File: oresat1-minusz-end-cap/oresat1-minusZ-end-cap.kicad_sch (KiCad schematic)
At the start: 36 parts, among them J1 M55-7011242R, J2 U.FL-R-SMA

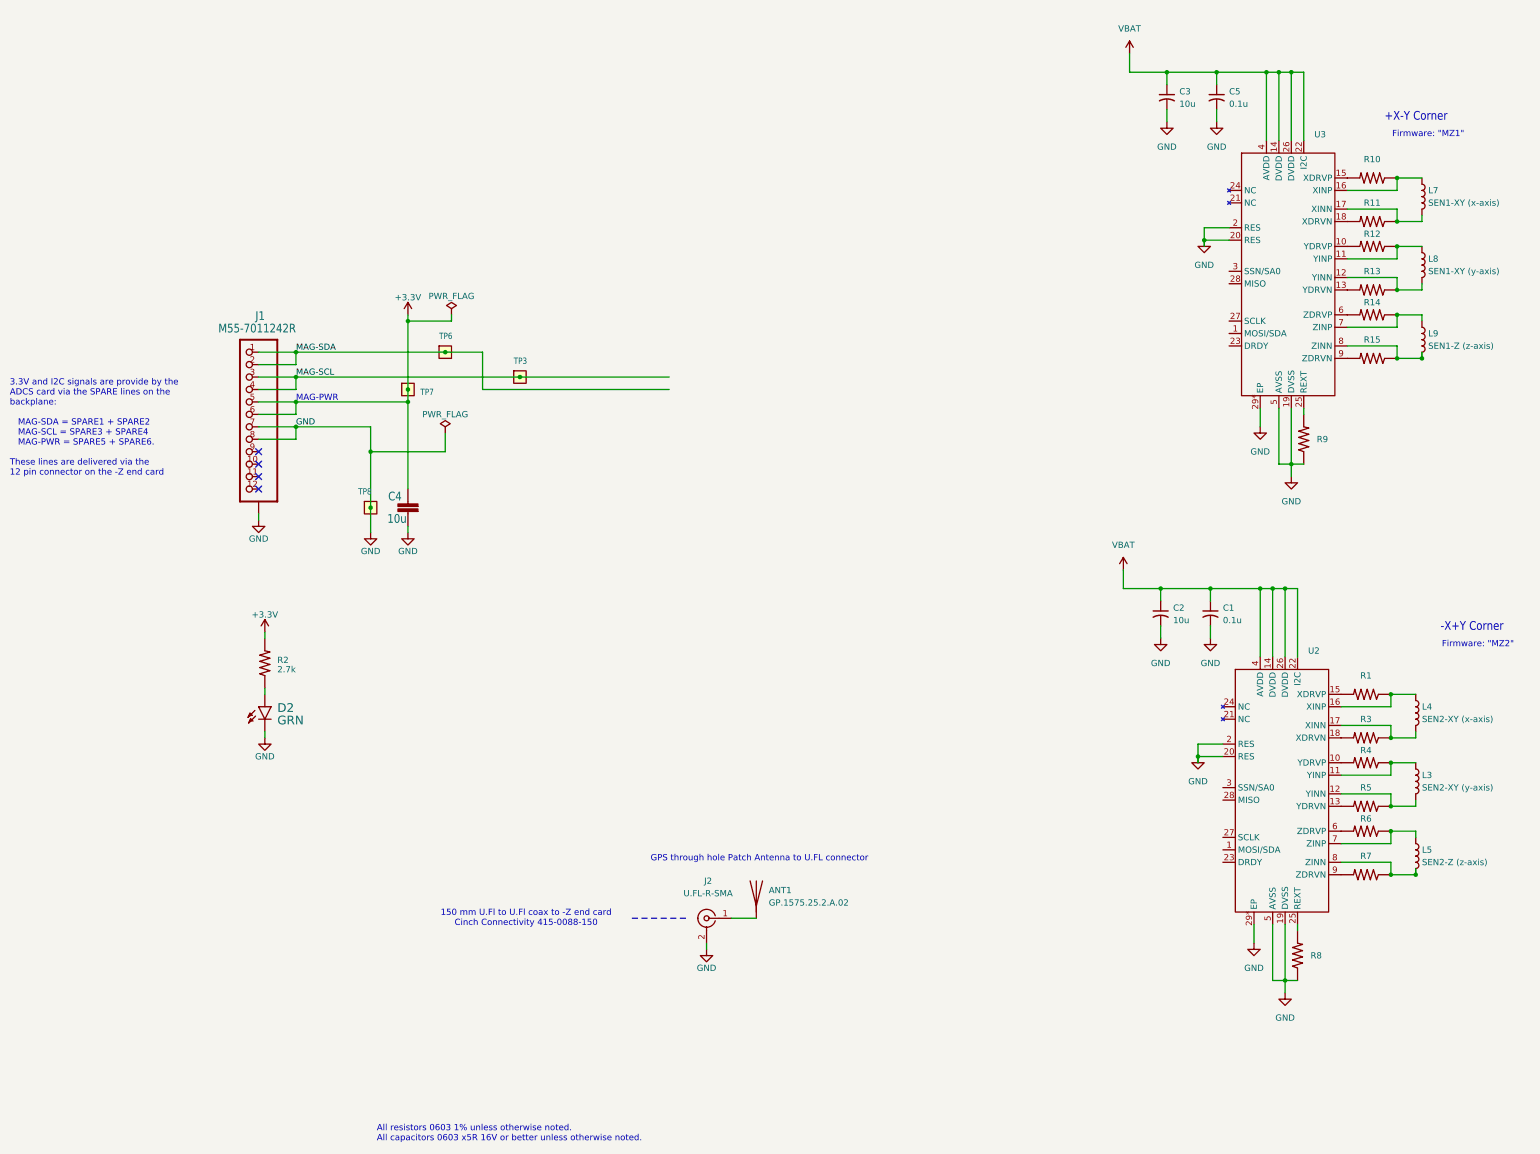
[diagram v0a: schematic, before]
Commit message: RM 3100 board layout
Round 1 - awaiting design review. Some issues with GND pads; DRC is clean, but looks weird. Debating if U1 needs to be further in the corner, therefore change its layout completely.
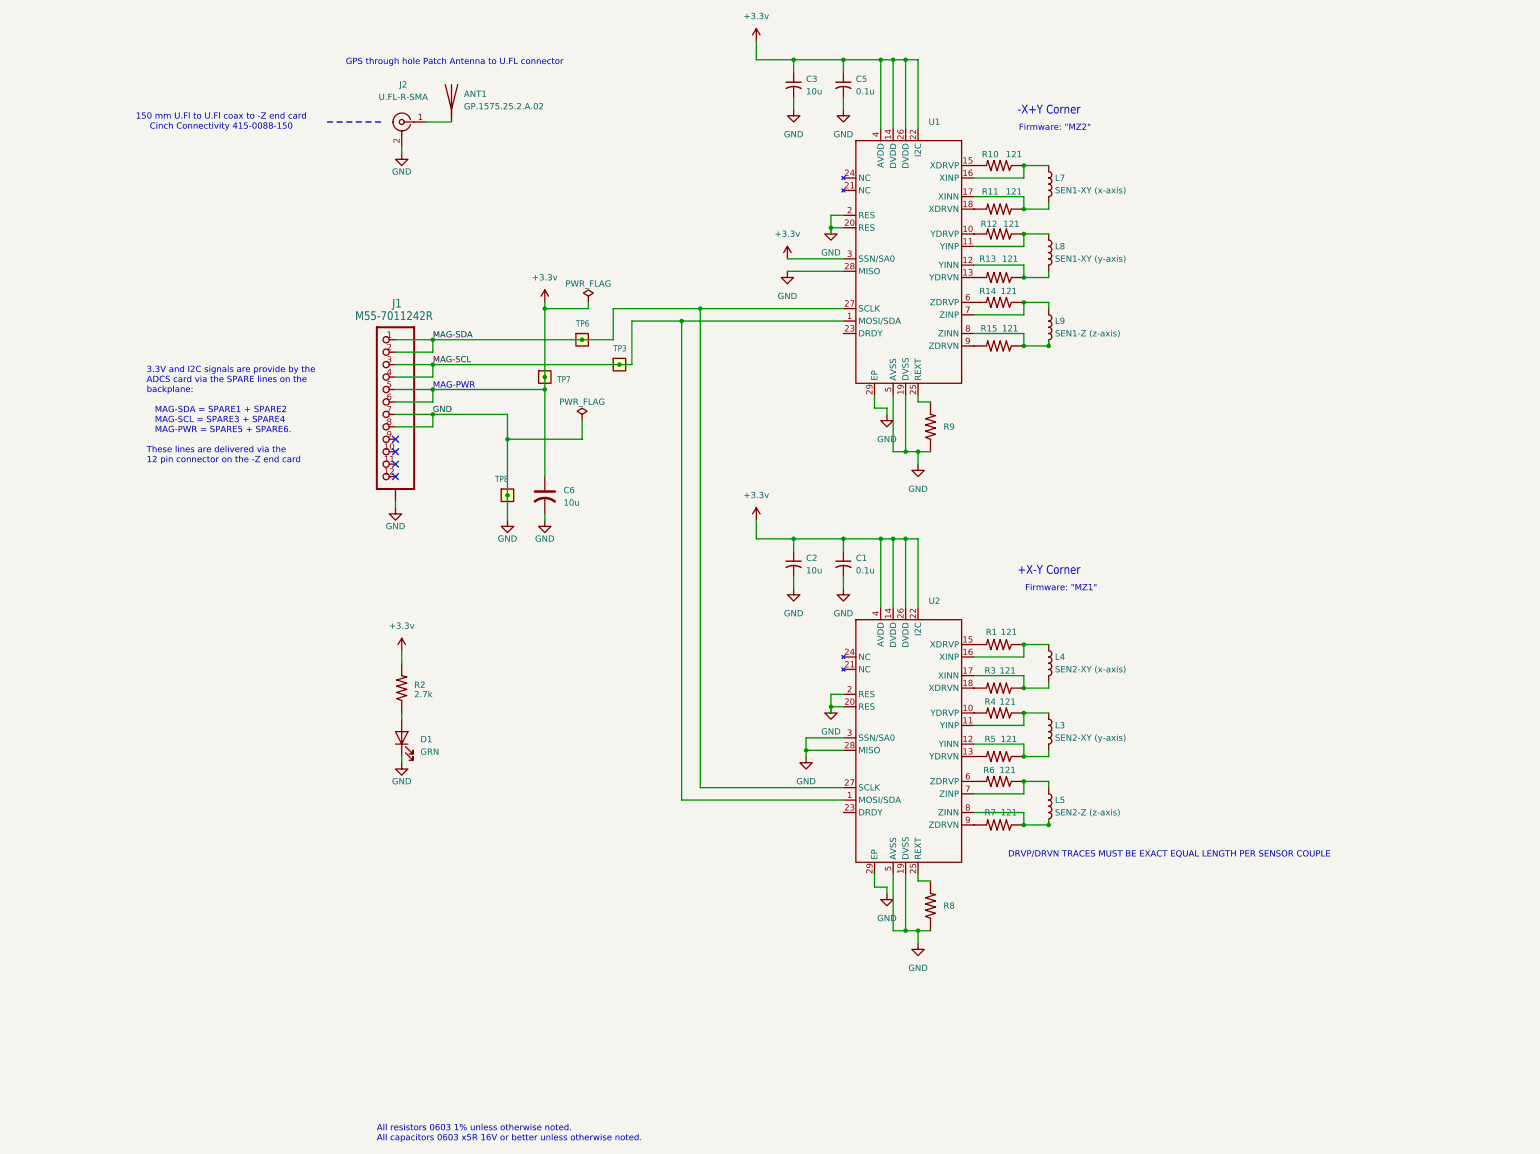
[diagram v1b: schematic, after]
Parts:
- removed C4: 10u, oresat-passives:0603-C-NOSILK, symbol oresat0.5-minusz-end-cap-eagle-import:C-EU0603-B-NOSILK
- removed D2: GRN, oresat-diodes:LED-0603, symbol oresat0.5-minusz-end-cap-eagle-import:LED-GREEN0603
- added C6: 10u, oresat-passives:0603-C-NOSILK, symbol Device:C_US
- added D1: GRN, oresat-passives:0603-C-NOSILK, symbol Device:LED
- C1, C2, C3, C5: footprint (none) -> oresat-passives:0603-C-NOSILK
- L3, L4, L7, L8: footprint (none) -> oresat-misc:RM3100 SEN-XY-f
- L5, L9: footprint (none) -> oresat-misc:RM3100 SEN-Z-f
- R1, R10, R11, R12, R13, R14, R15, R3, R4, R5, R6, R7: value ~ -> 121
- U1: renamed from U3; footprint (none) -> oresat-misc:RM3100-MagI2C
- U2: footprint (none) -> oresat-misc:RM3100-MagI2C
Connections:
- net +3.3V is gone; now on net +3.3v: J1.5, J1.6, R2.2, TP7.1
- net VBAT is gone; now on net +3.3v: C1.1, C2.1, C3.1, C5.1, U1.14 (DVDD), U1.22 (I2C), U1.26 (DVDD), U1.4 (AVDD), U2.14 (DVDD), U2.22 (I2C), U2.26 (DVDD), U2.4 (AVDD)
- net GND: now also U1.28 (MISO), U1.29 (EP), U2.28 (MISO), U2.29 (EP), U2.3 (SSN/SA0), C6.2, D1.1 (K); no longer U1.29* (EP), U2.29* (EP)
- net MAG-SCL: now also U1.1 (MOSI/SDA), U2.1 (MOSI/SDA)
- net MAG-SDA: now also U1.27 (SCLK), U2.27 (SCLK)
- net at R2.1: now also D1.2 (A)
- net +3.3v: now reaches U1.3 (SSN/SA0)
- net +3.3v: now also C6.1
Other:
- note added: "DRVP/DRVN TRACES MUST BE EXACT EQUAL LENGTH PER SENSOR COUPLE"
- moved on the sheet: ANT1, C1, C2, C3, C5, J1, J2, L3, L4, L5, L7, L8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

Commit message: Polishing the schematic and layout
Cleaned up ERCs, lots of OCD polishing for no reason, added 3.3V zone, cleaned up 3.3V routing.
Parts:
- added C4, C7: 100n, oresat-passives:0603-C-NOSILK, symbol Device:C_Small
- C1, C5: value 0.1u -> 100n; symbol Device:C_Small_US -> Device:C_Small
- C2: value 10u -> ~; footprint oresat-passives:0603-C-NOSILK -> oresat-passives:0805-C-NOSILK; symbol Device:C_Small_US -> Device:C_Small
- C3: footprint oresat-passives:0603-C-NOSILK -> oresat-passives:0805-C-NOSILK; symbol Device:C_Small_US -> Device:C_Small
- C6: footprint oresat-passives:0603-C-NOSILK -> oresat-passives:0805-C-NOSILK; symbol Device:C_US -> Device:C_Small
- J1: symbol oresat0.5-minusz-end-cap-eagle-import:J-HARWIN-M55-70X1242R -> oresat-connectors:J-HARWIN-M55-6001242R
- R8, R9: value ~ -> 33k
- U1, U2: value ~ -> RM3100
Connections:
- net +3.3v: now also U1.28 (MISO), C4.1, C7.1; no longer U1.3 (SSN/SA0)
- net GND: now also J1.SH (SHIELD), U1.3 (SSN/SA0), C4.2, C7.2; no longer J1.P$1 (SHIELDS), J1.P$2 (SHIELDS), J1.P$3 (SHIELDS), J1.P$4 (SHIELDS), U1.28 (MISO)
- no-connect marks 4 -> 6
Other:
- note added: "Address: 00"
- note added: "Address: 01"
- moved on the sheet: C1, C2, C3, J1

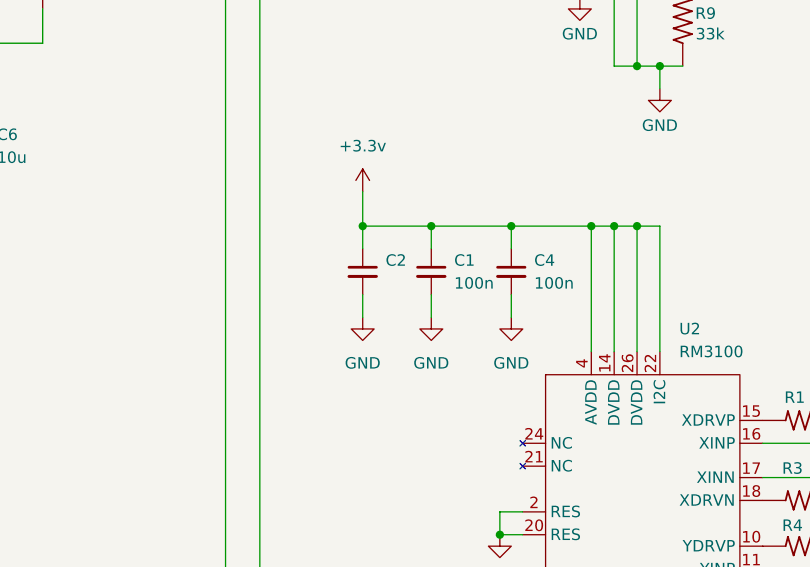
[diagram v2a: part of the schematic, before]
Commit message: Fix BOM and add 3D of antenna.
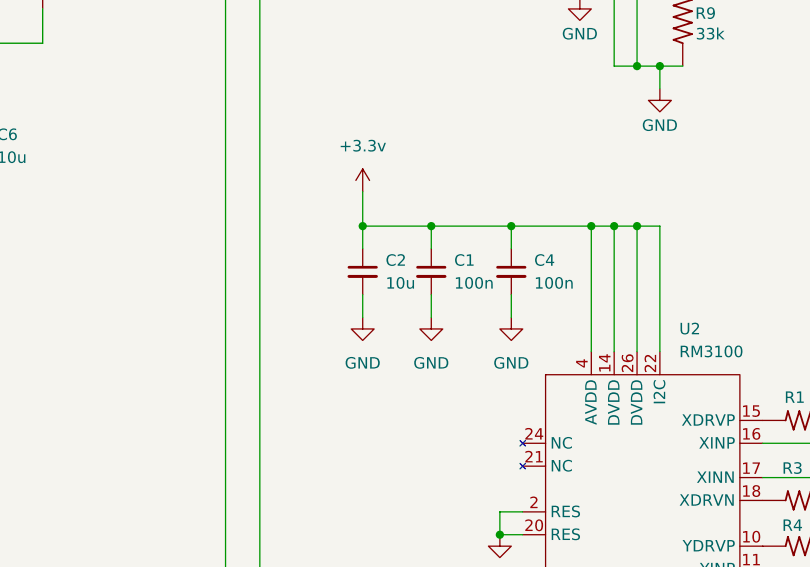
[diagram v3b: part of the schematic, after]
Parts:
- ANT1, J1, J2: DIS (none) -> DigiKey; DST Digi-Key -> (none)
- C1, C4, C5, C7: DIS (none) -> DigiKey; DPN (none) -> 399-6856-1-ND; MFR (none) -> KEMET; MPN (none) -> C0603C104K5RACAUTO
- C2: value ~ -> 10u; DIS (none) -> DigiKey; DPN (none) -> 490-GRT21BC71E106KE13KCT-ND; MFR (none) -> Murata Electronics; MPN (none) -> GRT21BC71E106KE13K
- C3, C6: DIS (none) -> DigiKey; DPN (none) -> 490-GRT21BC71E106KE13KCT-ND; MFR (none) -> Murata Electronics; MPN (none) -> GRT21BC71E106KE13K
- D1: DIS (none) -> DigiKey; DPN (none) -> 732-4971-1-ND; MFR (none) -> Wurth; MPN (none) -> 150060GS75000
- L3, L4, L5, L7, L8, L9: DIS (none) -> PNI
- R1, R10, R11, R12, R13, R14, R15, R3, R4, R5, R6, R7: DIS (none) -> DigiKey; DPN (none) -> RMCF0603FT121RCT-ND; MFR (none) -> Stackpole Electronics; MPN (none) -> RMCF0603FT121R
- R2: DIS (none) -> DigiKey; DPN (none) -> RMCF0603FT2K70CT-ND; MFR (none) -> Stackpole Electronics; MPN (none) -> RMCF0603FT2K70
- R8, R9: DIS (none) -> DigiKey; DPN (none) -> RMCF0603FT33K0CT-ND; MFR (none) -> Stackpole Electronics; MPN (none) -> RMCF0603FT33K0
- TP3, TP6, TP7, TP8: DST N/A -> (none)
- U1, U2: DIS (none) -> PNI; DPN (none) -> RM3100

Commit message: New -Z DFX
Added new DFX to edge.cuts and User.comments. Antenna footprint warning - juts out over cut.
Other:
- title: OreSat1 +Z End Cap -> OreSat1 -Z End Cap
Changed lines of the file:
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@@
 	(paper "B")
 	(title_block
-		(title "OreSat1 +Z End Cap")
+		(title "OreSat1 -Z End Cap")
 		(date "2026-01-21")
 		(rev "1.0")
